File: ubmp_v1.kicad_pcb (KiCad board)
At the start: 2 copper layers, 33.5 x 14 mm, 22 parts, among them J1 M20-9760542, J2 1001-011-01101, U1 NUF8401MNT4G, U2 MIC5245-3.3YM5, U3 STM32F103CBU6, U4 NUF2042XV6T1G, Y1 PRQC8.00CR1010V00L

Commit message: Added OSHW logo
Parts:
- added REF**: OSHW-Symbol_6.7x6mm_SilkScreen, Symbol:OSHW-Symbol_6.7x6mm_SilkScreen, B.Cu at (105.0, 102.5)
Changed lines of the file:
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@@
     (tracks 330)
     (zones 0)
-    (modules 22)
+    (modules 23)
     (nets 57)
   )
@@
       (net 3 +5V))
   )
+  (module Symbol:OSHW-Symbol_6.7x6mm_SilkScreen (layer B.Cu)
+    (at 105 102.5 180)
+    (descr "Open Source Hardware Symbol")
+    (tags "Logo Symbol OSHW")
+    (attr virtual)
+    (fp_text reference REF** (at 0 0 180) (layer B.SilkS) hide
+      (effects (font (size 1 1) (thickness 0.15)) (justify mirror))
+    )
+    (fp_text value OSHW-Symbol_6.7x6mm_SilkScreen (at 0.75 0 180) (layer B.Fab) hide
+      (effects (font (size 1 1) (thickness 0.15)) (justify mirror))
+    )
+    (fp_poly (pts (xy 0.555814 2.531069) (xy 0.639635 2.086445) (xy 0.94892 1.958947) (xy 1.258206 1.831449)
+      (xy 1.629246 2.083754) (xy 1.733157 2.154004) (xy 1.827087 2.216728) (xy 1.906652 2.269062)
+      (xy 1.96747 2.308143) (xy 2.005157 2.331107) (xy 2.015421 2.336058) (xy 2.03391 2.323324)
+      (xy 2.07342 2.288118) (xy 2.129522 2.234938) (xy 2.197787 2.168282) (xy 2.273786 2.092646)
+      (xy 2.353092 2.012528) (xy 2.431275 1.932426) (xy 2.503907 1.856836) (xy 2.566559 1.790255)
+      (xy 2.614803 1.737182) (xy 2.64421 1.702113) (xy 2.651241 1.690377) (xy 2.641123 1.66874)
+      (xy 2.612759 1.621338) (xy 2.569129 1.552807) (xy 2.513218 1.467785) (xy 2.448006 1.370907)
+      (xy 2.410219 1.31565) (xy 2.341343 1.214752) (xy 2.28014 1.123701) (xy 2.229578 1.04703)
+      (xy 2.192628 0.989272) (xy 2.172258 0.954957) (xy 2.169197 0.947746) (xy 2.176136 0.927252)
+      (xy 2.195051 0.879487) (xy 2.223087 0.811168) (xy 2.257391 0.729011) (xy 2.295109 0.63973)
+      (xy 2.333387 0.550042) (xy 2.36937 0.466662) (xy 2.400206 0.396306) (xy 2.423039 0.34569)
+      (xy 2.435017 0.321529) (xy 2.435724 0.320578) (xy 2.454531 0.315964) (xy 2.504618 0.305672)
+      (xy 2.580793 0.290713) (xy 2.677865 0.272099) (xy 2.790643 0.250841) (xy 2.856442 0.238582)
+      (xy 2.97695 0.215638) (xy 3.085797 0.193805) (xy 3.177476 0.174278) (xy 3.246481 0.158252)
+      (xy 3.287304 0.146921) (xy 3.295511 0.143326) (xy 3.303548 0.118994) (xy 3.310033 0.064041)
+      (xy 3.31497 -0.015108) (xy 3.318364 -0.112026) (xy 3.320218 -0.220287) (xy 3.320538 -0.333465)
+      (xy 3.319327 -0.445135) (xy 3.31659 -0.548868) (xy 3.312331 -0.638241) (xy 3.306555 -0.706826)
+      (xy 3.299267 -0.748197) (xy 3.294895 -0.75681) (xy 3.268764 -0.767133) (xy 3.213393 -0.781892)
+      (xy 3.136107 -0.799352) (xy 3.04423 -0.81778) (xy 3.012158 -0.823741) (xy 2.857524 -0.852066)
+      (xy 2.735375 -0.874876) (xy 2.641673 -0.89308) (xy 2.572384 -0.907583) (xy 2.523471 -0.919292)
+      (xy 2.490897 -0.929115) (xy 2.470628 -0.937956) (xy 2.458626 -0.946724) (xy 2.456947 -0.948457)
+      (xy 2.440184 -0.976371) (xy 2.414614 -1.030695) (xy 2.382788 -1.104777) (xy 2.34726 -1.191965)
+      (xy 2.310583 -1.285608) (xy 2.275311 -1.379052) (xy 2.243996 -1.465647) (xy 2.219193 -1.53874)
+      (xy 2.203454 -1.591678) (xy 2.199332 -1.617811) (xy 2.199676 -1.618726) (xy 2.213641 -1.640086)
+      (xy 2.245322 -1.687084) (xy 2.291391 -1.754827) (xy 2.348518 -1.838423) (xy 2.413373 -1.932982)
+      (xy 2.431843 -1.959854) (xy 2.497699 -2.057275) (xy 2.55565 -2.146163) (xy 2.602538 -2.221412)
+      (xy 2.635207 -2.27792) (xy 2.6505 -2.310581) (xy 2.651241 -2.314593) (xy 2.638392 -2.335684)
+      (xy 2.602888 -2.377464) (xy 2.549293 -2.435445) (xy 2.482171 -2.505135) (xy 2.406087 -2.582045)
+      (xy 2.325604 -2.661683) (xy 2.245287 -2.739561) (xy 2.169699 -2.811186) (xy 2.103405 -2.87207)
+      (xy 2.050969 -2.917721) (xy 2.016955 -2.94365) (xy 2.007545 -2.947883) (xy 1.985643 -2.937912)
+      (xy 1.9408 -2.91102) (xy 1.880321 -2.871736) (xy 1.833789 -2.840117) (xy 1.749475 -2.782098)
+      (xy 1.649626 -2.713784) (xy 1.549473 -2.645579) (xy 1.495627 -2.609075) (xy 1.313371 -2.4858)
+      (xy 1.160381 -2.56852) (xy 1.090682 -2.604759) (xy 1.031414 -2.632926) (xy 0.991311 -2.648991)
+      (xy 0.981103 -2.651226) (xy 0.968829 -2.634722) (xy 0.944613 -2.588082) (xy 0.910263 -2.515609)
+      (xy 0.867588 -2.421606) (xy 0.818394 -2.310374) (xy 0.76449 -2.186215) (xy 0.707684 -2.053432)
+      (xy 0.649782 -1.916327) (xy 0.592593 -1.779202) (xy 0.537924 -1.646358) (xy 0.487584 -1.522098)
+      (xy 0.44338 -1.410725) (xy 0.407119 -1.316539) (xy 0.380609 -1.243844) (xy 0.365658 -1.196941)
+      (xy 0.363254 -1.180833) (xy 0.382311 -1.160286) (xy 0.424036 -1.126933) (xy 0.479706 -1.087702)
+      (xy 0.484378 -1.084599) (xy 0.628264 -0.969423) (xy 0.744283 -0.835053) (xy 0.83143 -0.685784)
+      (xy 0.888699 -0.525913) (xy 0.915086 -0.359737) (xy 0.909585 -0.191552) (xy 0.87119 -0.025655)
+      (xy 0.798895 0.133658) (xy 0.777626 0.168513) (xy 0.666996 0.309263) (xy 0.536302 0.422286)
+      (xy 0.390064 0.506997) (xy 0.232808 0.562806) (xy 0.069057 0.589126) (xy -0.096667 0.58537)
+      (xy -0.259838 0.55095) (xy -0.415935 0.485277) (xy -0.560433 0.387765) (xy -0.605131 0.348187)
+      (xy -0.718888 0.224297) (xy -0.801782 0.093876) (xy -0.858644 -0.052315) (xy -0.890313 -0.197088)
+      (xy -0.898131 -0.35986) (xy -0.872062 -0.52344) (xy -0.814755 -0.682298) (xy -0.728856 -0.830906)
+      (xy -0.617014 -0.963735) (xy -0.481877 -1.075256) (xy -0.464117 -1.087011) (xy -0.40785 -1.125508)
+      (xy -0.365077 -1.158863) (xy -0.344628 -1.18016) (xy -0.344331 -1.180833) (xy -0.348721 -1.203871)
+      (xy -0.366124 -1.256157) (xy -0.394732 -1.33339) (xy -0.432735 -1.431268) (xy -0.478326 -1.545491)
+      (xy -0.529697 -1.671758) (xy -0.585038 -1.805767) (xy -0.642542 -1.943218) (xy -0.700399 -2.079808)
+      (xy -0.756802 -2.211237) (xy -0.809942 -2.333205) (xy -0.85801 -2.441409) (xy -0.899199 -2.531549)
+      (xy -0.931699 -2.599323) (xy -0.953703 -2.64043) (xy -0.962564 -2.651226) (xy -0.98964 -2.642819)
+      (xy -1.040303 -2.620272) (xy -1.105817 -2.587613) (xy -1.141841 -2.56852) (xy -1.294832 -2.4858)
+      (xy -1.477088 -2.609075) (xy -1.570125 -2.672228) (xy -1.671985 -2.741727) (xy -1.767438 -2.807165)
+      (xy -1.81525 -2.840117) (xy -1.882495 -2.885273) (xy -1.939436 -2.921057) (xy -1.978646 -2.942938)
+      (xy -1.991381 -2.947563) (xy -2.009917 -2.935085) (xy -2.050941 -2.900252) (xy -2.110475 -2.846678)
+      (xy -2.184542 -2.777983) (xy -2.269165 -2.697781) (xy -2.322685 -2.646286) (xy -2.416319 -2.554286)
+      (xy -2.497241 -2.471999) (xy -2.562177 -2.402945) (xy -2.607858 -2.350644) (xy -2.631011 -2.318616)
+      (xy -2.633232 -2.312116) (xy -2.622924 -2.287394) (xy -2.594439 -2.237405) (xy -2.550937 -2.167212)
+      (xy -2.495577 -2.081875) (xy -2.43152 -1.986456) (xy -2.413303 -1.959854) (xy -2.346927 -1.863167)
+      (xy -2.287378 -1.776117) (xy -2.237984 -1.703595) (xy -2.202075 -1.650493) (xy -2.182981 -1.621703)
+      (xy -2.181136 -1.618726) (xy -2.183895 -1.595782) (xy -2.198538 -1.545336) (xy -2.222513 -1.474041)
+      (xy -2.253266 -1.388547) (xy -2.288244 -1.295507) (xy -2.324893 -1.201574) (xy -2.360661 -1.113399)
+      (xy -2.392994 -1.037634) (xy -2.419338 -0.980931) (xy -2.437142 -0.949943) (xy -2.438407 -0.948457)
+      (xy -2.449294 -0.939601) (xy -2.467682 -0.930843) (xy -2.497606 -0.921277) (xy -2.543103 -0.909996)
+      (xy -2.608209 -0.896093) (xy -2.696961 -0.878663) (xy -2.813393 -0.856798) (xy -2.961542 -0.829591)
+      (xy -2.993618 -0.823741) (xy -3.088686 -0.805374) (xy -3.171565 -0.787405) (xy -3.23493 -0.771569)
+      (xy -3.271458 -0.7596) (xy -3.276356 -0.75681) (xy -3.284427 -0.732072) (xy -3.290987 -0.67679)
+      (xy -3.296033 -0.597389) (xy -3.299559 -0.500296) (xy -3.301561 -0.391938) (xy -3.302036 -0.27874)
+      (xy -3.300977 -0.167128) (xy -3.298382 -0.063529) (xy -3.294246 0.025632) (xy -3.288563 0.093928)
+      (xy -3.281331 0.134934) (xy -3.276971 0.143326) (xy -3.252698 0.151792) (xy -3.197426 0.165565)
+      (xy -3.116662 0.18345) (xy -3.015912 0.204252) (xy -2.900683 0.226777) (xy -2.837902 0.238582)
+      (xy -2.718787 0.260849) (xy -2.612565 0.281021) (xy -2.524427 0.298085) (xy -2.459566 0.311031)
+      (xy -2.423174 0.318845) (xy -2.417184 0.320578) (xy -2.407061 0.34011) (xy -2.385662 0.387157)
+      (xy -2.355839 0.454997) (xy -2.320445 0.536909) (xy -2.282332 0.626172) (xy -2.244353 0.716065)
+      (xy -2.20936 0.799865) (xy -2.180206 0.870853) (xy -2.159743 0.922306) (xy -2.150823 0.947503)
+      (xy -2.150657 0.948604) (xy -2.160769 0.968481) (xy -2.189117 1.014223) (xy -2.232723 1.081283)
+      (xy -2.288606 1.165116) (xy -2.353787 1.261174) (xy -2.391679 1.31635) (xy -2.460725 1.417519)
+      (xy -2.52205 1.50937) (xy -2.572663 1.587256) (xy -2.609571 1.646531) (xy -2.629782 1.682549)
+      (xy -2.632701 1.690623) (xy -2.620153 1.709416) (xy -2.585463 1.749543) (xy -2.533063 1.806507)
+      (xy -2.467384 1.875815) (xy -2.392856 1.952969) (xy -2.313913 2.033475) (xy -2.234983 2.112837)
+      (xy -2.1605 2.18656) (xy -2.094894 2.250148) (xy -2.042596 2.299106) (xy -2.008039 2.328939)
+      (xy -1.996478 2.336058) (xy -1.977654 2.326047) (xy -1.932631 2.297922) (xy -1.865787 2.254546)
+      (xy -1.781499 2.198782) (xy -1.684144 2.133494) (xy -1.610707 2.083754) (xy -1.239667 1.831449)
+      (xy -0.621095 2.086445) (xy -0.537275 2.531069) (xy -0.453454 2.975693) (xy 0.471994 2.975693)
+      (xy 0.555814 2.531069)) (layer B.SilkS) (width 0.01))
+  )
   (gr_line (start 85 100) (end 85 112) (layer Edge.Cuts) (width 0.15))

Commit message: v1.3 release
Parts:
- removed REF**: OSHW-Symbol_6.7x6mm_SilkScreen, Symbol:OSHW-Symbol_6.7x6mm_SilkScreen
- added D2: LTST-C191KGKT, leds:LEDC1608X60, F.Cu at (110.6, 111.1)
- added R2: 470, passive:R_0402_1005Metric_Rounded, F.Cu at (110.6, 110.0)
- moved Y1 0.36 mm to (101.2, 111.2)
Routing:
- net Net-(F1-Pad1): track 21.4 -> 23.7 mm, vias 2 -> 3
- net Net-(D2-Pad2): track 0.00 -> 1.22 mm
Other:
- board text added: "µBMP v1.3"
- board text removed: "µBMP v1.2"

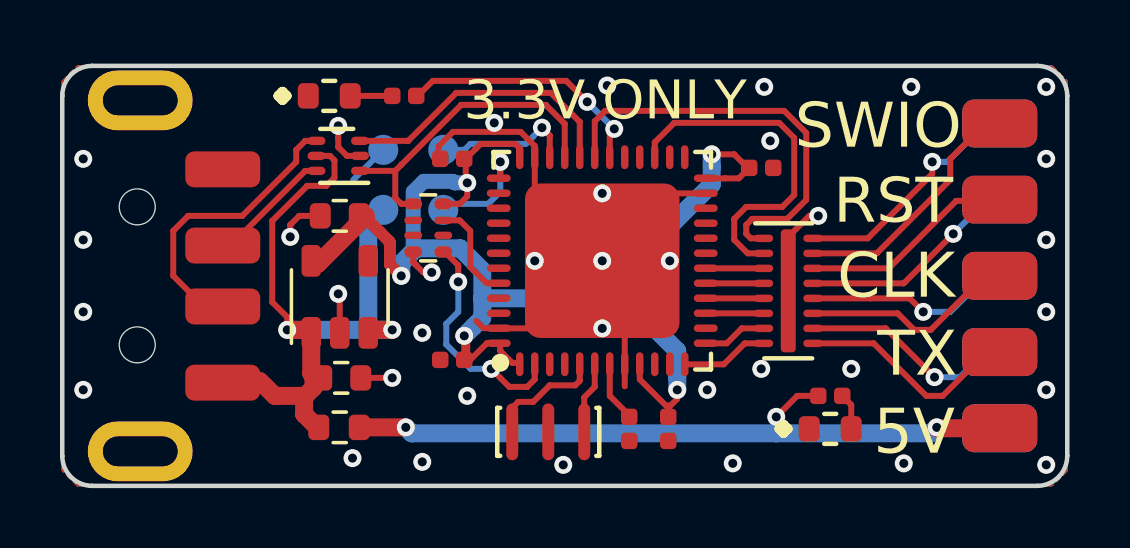
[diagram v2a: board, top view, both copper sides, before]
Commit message: Moved to USB-C plug
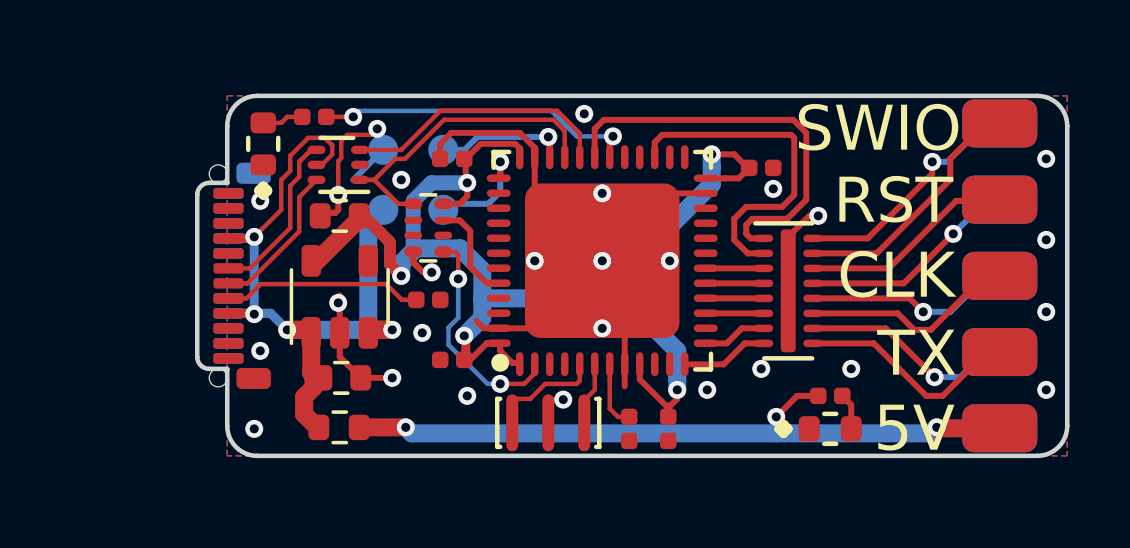
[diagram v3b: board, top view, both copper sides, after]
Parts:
- removed J2: 1001-011-01101, usb:USB_A_1001-011-01101
- added P1: USB_C_Plug, usb:USB_C_Plug_Molex_1054440001, F.Cu at (90.5, 106.0)
- added R3: 5.1k, passive:R_0402_1005Metric_Rounded, F.Cu at (97.2, 106.8)
- moved R1 3.08 mm to (93.4, 100.7)
- moved D1 2.72 mm to (91.7, 101.6), turned to 90 degrees
- moved U4 0.30 mm to (94.2, 102.3)
- moved Y1 0.30 mm to (101.2, 110.9)
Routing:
- net Net-(P1-PadA5): track 0.00 -> 6.67 mm
- net +5V: track 22.6 -> 26.9 mm, vias 2 -> 4
- net /DM: track 9.82 -> 5.68 mm
- net GND: track 33.8 -> 37.2 mm, vias 36 -> 27
- net /DP: track 4.16 -> 5.04 mm
- net /bmp_core/LED_STLINK: track 10.1 -> 10.7 mm
- net /bmp_core/DM_P: track 9.57 -> 8.97 mm
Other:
- board size 33.5 x 14 mm -> 29 x 12 mm
- net class Default: clearance 0.2 -> 0.15; trace_width 0.2 -> 0.15
- net class Power: clearance 0.2 -> 0.15
- rule trace_clearance: 0.2 -> 0.15
- rule trace_min: 0.2 -> 0.15
- board text added: "µBMP v1.4"
- board text removed: "SWD PROG"
- board text removed: "µBMP v1.3"

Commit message: Reinforced the USB-C anchor pads
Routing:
- net GND: vias 27 -> 30
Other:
- outline, holes or cut-outs redrawn
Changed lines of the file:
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@@
     (thickness 0.7)
     (drawings 33)
-    (tracks 355)
+    (tracks 358)
     (zones 0)
     (modules 25)
@@
     (last_trace_width 0.15)
     (trace_clearance 0.15)
-    (zone_clearance 0.508)
-    (zone_45_only yes)
+    (zone_clearance 0.2)
+    (zone_45_only no)
     (trace_min 0.15)
     (segment_width 0.15)
@@
       (effects (font (size 1 1) (thickness 0.1)))
     )
-    (pad "" np_thru_hole circle (at 3.4 -0.3 90) (size 0.6 0.6) (drill 0.6) (layers *.Cu))
-    (pad "" np_thru_hole circle (at -3.4 -0.3 90) (size 0.6 0.6) (drill 0.6) (layers *.Cu))
+    (pad "" np_thru_hole circle (at 3.35 -0.3 90) (size 0.6 0.6) (drill 0.6) (layers *.Cu))
+    (pad "" np_thru_hole circle (at -3.35 -0.3 90) (size 0.6 0.6) (drill 0.6) (layers *.Cu))
     (pad B12 smd roundrect (at -2.75 0.04 90) (size 0.35 1) (layers B.Cu B.Paste B.Mask) (roundrect_rratio 0.25)
       (net 2 GND))
@@
   (gr_arc (start 91.5 101) (end 91.5 100) (angle -90) (layer Edge.Cuts) (width 0.15))
   (gr_arc (start 91.5 111) (end 90.5 111) (angle -90) (layer Edge.Cuts) (width 0.15))
-  (gr_arc (start 89.9 108.7) (end 89.5 108.7) (angle -90) (layer Edge.Cuts) (width 0.15))
-  (gr_arc (start 89.9 103.3) (end 89.9 102.9) (angle -90) (layer Edge.Cuts) (width 0.15))
-  (gr_line (start 90.5 109.1) (end 90.5 111) (layer Edge.Cuts) (width 0.15))
-  (gr_line (start 89.9 109.1) (end 90.5 109.1) (layer Edge.Cuts) (width 0.15))
-  (gr_line (start 89.5 103.3) (end 89.5 108.7) (layer Edge.Cuts) (width 0.15))
-  (gr_line (start 90.5 102.9) (end 89.9 102.9) (layer Edge.Cuts) (width 0.15))
-  (gr_line (start 90.5 101) (end 90.5 102.9) (layer Edge.Cuts) (width 0.15))
+  (gr_arc (start 89.95 108.65) (end 89.55 108.65) (angle -90) (layer Edge.Cuts) (width 0.15))
+  (gr_arc (start 89.95 103.35) (end 89.95 102.95) (angle -90) (layer Edge.Cuts) (width 0.15))
+  (gr_line (start 90.5 109.05) (end 90.5 111) (layer Edge.Cuts) (width 0.15))
+  (gr_line (start 89.95 109.05) (end 90.5 109.05) (layer Edge.Cuts) (width 0.15))
+  (gr_line (start 89.55 103.35) (end 89.55 108.65) (layer Edge.Cuts) (width 0.15))
+  (gr_line (start 90.5 102.95) (end 89.95 102.95) (layer Edge.Cuts) (width 0.15))
+  (gr_line (start 90.5 101) (end 90.5 102.95) (layer Edge.Cuts) (width 0.15))
   (gr_arc (start 117.5 111) (end 117.5 112) (angle -90) (layer Edge.Cuts) (width 0.15))
   (gr_arc (start 117.5 101) (end 118.5 101) (angle -90) (layer Edge.Cuts) (width 0.15))
@@
   (segment (start 101.2 110.024264) (end 101.2 110.049274) (width 0.15) (layer F.Cu) (net 2))
   (via (at 101.7 110.12501) (size 0.6) (drill 0.3) (layers F.Cu B.Cu) (net 2))
-  (via (at 91.6 108.5) (size 0.6) (drill 0.3) (layers F.Cu B.Cu) (net 2))
+  (via (at 91.6 108.75) (size 0.6) (drill 0.3) (layers F.Cu B.Cu) (net 2))
   (segment (start 94.25 108.7) (end 94.25 107.9) (width 0.2) (layer F.Cu) (net 2))
   (segment (start 94.95 109.4) (end 94.25 108.7) (width 0.2) (layer F.Cu) (net 2))
   (via (at 94.2 103.3) (size 0.6) (drill 0.3) (layers F.Cu B.Cu) (net 2))
   (segment (start 93.6 104) (end 93.6 103.9) (width 0.15) (layer F.Cu) (net 2))
-  (via (at 91.6 103.5) (size 0.6) (drill 0.3) (layers F.Cu B.Cu) (net 2))
+  (via (at 91.6 103.2) (size 0.6) (drill 0.3) (layers F.Cu B.Cu) (net 2))
   (segment (start 94.2 103.8) (end 94.2 103.3) (width 0.2) (layer F.Cu) (net 2))
   (segment (start 93.6 103.9) (end 94.1 103.9) (width 0.2) (layer F.Cu) (net 2))
@@
   (segment (start 100.253724 101.234483) (end 97.965517 101.234483) (width 0.2) (layer F.Cu) (net 2))
   (segment (start 100.75 101.730759) (end 100.253724 101.234483) (width 0.2) (layer F.Cu) (net 2))
+  (via (at 91.6 110.1) (size 0.6) (drill 0.3) (layers F.Cu B.Cu) (net 2))
+  (via (at 92.3 109.4) (size 0.6) (drill 0.3) (layers F.Cu B.Cu) (net 2))
+  (via (at 91.1 101.7) (size 0.6) (drill 0.3) (layers F.Cu B.Cu) (net 2))
   (segment (start 93.45 109.4) (end 93.3 109.25) (width 0.6) (layer F.Cu) (net 3))
   (segment (start 93.3 109.25) (end 93.3 107.9) (width 0.6) (layer F.Cu) (net 3))
@@
       )
     )
+  )
+  (zone (net 2) (net_name GND) (layer F.Cu) (hatch edge 0.508)
+    (connect_pads yes (clearance 0.2))
+    (min_thickness 0.2)
+    (fill yes (arc_segments 16) (thermal_gap 0.2) (thermal_bridge_width 0.2))
+    (polygon
+      (pts
+        (xy 90.5 110.2) (xy 92.2 110.2) (xy 92.2 108.8) (xy 91.3 108.8) (xy 91.3 109.1)
+        (xy 90.5 109.1)
+      )
+    )
+  )
+  (zone (net 2) (net_name GND) (layer B.Cu) (hatch edge 0.508)
+    (connect_pads yes (clearance 0.2))
+    (min_thickness 0.2)
+    (fill yes (arc_segments 16) (thermal_gap 0.2) (thermal_bridge_width 0.2))
+    (polygon
+      (pts
+        (xy 90.5 101.8) (xy 92.2 101.8) (xy 92.2 103.2) (xy 91.3 103.2) (xy 91.3 102.9)
+        (xy 90.5 102.9)
+      )
+    )

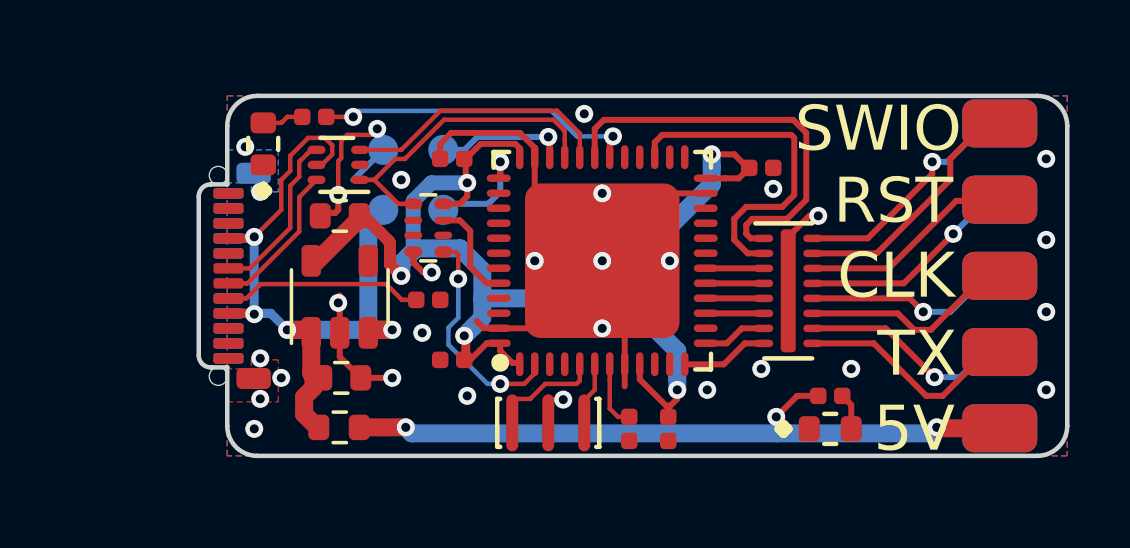
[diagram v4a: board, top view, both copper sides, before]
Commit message: Improved USB-C mounting even more
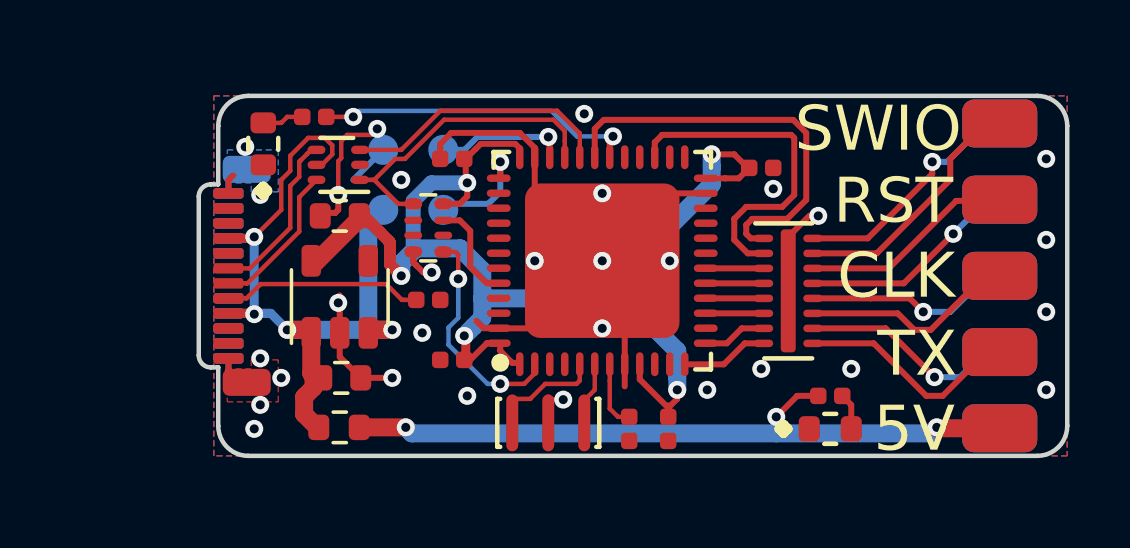
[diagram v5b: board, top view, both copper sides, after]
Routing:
- net GND: track 37.2 -> 41.3 mm
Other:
- outline, holes or cut-outs redrawn
- rule pad_to_mask_clearance: 0.08 -> 0.05
- rule solder_mask_min_width: 0.25 -> 0.07
